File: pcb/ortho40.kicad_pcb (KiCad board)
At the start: 2 copper layers, 284 x 84 mm, 129 parts, among them J1 SWD, J2 USB_C_Receptacle_USB2.0, SW1 SW_Push, U1 RP2040, U2 XC6206PxxxMR, U3 W25Q128JVS, U4 USBLC6-2SC6, U5 ST7735S_1.8inch, Y1 12MHz

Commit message: More changes...
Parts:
- removed C1: 100nF, Capacitor_SMD:C_0402_1005Metric
- added REF**: MountingHole_2.2mm_M2, MountingHole:MountingHole_2.2mm_M2, F.Cu at (60.1, 80.1)
- added REF**: MountingHole_2.2mm_M2, MountingHole:MountingHole_2.2mm_M2, F.Cu at (60.0, 40.1)
- added REF**: MountingHole_2.2mm_M2, MountingHole:MountingHole_2.2mm_M2, F.Cu at (300.1, 40.0)
- added REF**: MountingHole_2.2mm_M2, MountingHole:MountingHole_2.2mm_M2, F.Cu at (300.2, 80.3)
- moved R2 1.47 mm to (182.8, 32.8)
- moved R3 1.03 mm to (179.1, 32.8)
- renumbered MX8 to MX10, MX10 to MX11, MX15 to MX14, MX14 to MX15, MX19 to MX18, MX21 to MX19, MX3 to MX2, MX23 to MX20, MX18 to MX21, MX20 to MX22, MX22 to MX23, MX27 to MX26, MX26 to MX27, MX2 to MX3, MX31 to MX30, MX33 to MX31, MX35 to MX32, MX30 to MX33, MX32 to MX34, MX34 to MX35, MX39 to MX38, MX38 to MX39, MX43 to MX42, MX45 to MX43, MX47 to MX44, MX42 to MX45, MX44 to MX46, MX46 to MX47, MX7 to MX6, MX9 to MX7, MX11 to MX8, MX6 to MX9
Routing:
- net r0: track 305.8 -> 304.4 mm
- net Net-(R2-Pad1): track 15.2 -> 15.9 mm

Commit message: Missing connection...
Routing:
- net QSPI_SD1: track 28.0 -> 29.0 mm
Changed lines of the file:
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@@
   (segment (start 186.90639 40.401008) (end 186.907398 40.4) (width 0.2) (layer "B.Cu") (net 97))
   (segment (start 192 35) (end 188.635 31.635) (width 0.2) (layer "B.Cu") (net 97))
-  (segment (start 187 41) (end 182.2 45.8) (width 0.2) (layer "B.Cu") (net 98))
-  (segment (start 191.4625 30.3) (end 191.4625 29.394684) (width 0.2) (layer "B.Cu") (net 98))
-  (segment (start 192 34.434314) (end 191.4625 33.896814) (width 0.2) (layer "B.Cu") (net 98))
-  (segment (start 190 41) (end 187 41) (width 0.2) (layer "B.Cu") (net 98))
-  (segment (start 188.185153 28.814847) (end 187.49375 29.50625) (width 0.2) (layer "B.Cu") (net 98))
-  (segment (start 182.2 45.8) (end 182.2 46.5625) (width 0.2) (layer "B.Cu") (net 98))
-  (segment (start 192 34.434314) (end 192.4 34.834315) (width 0.2) (layer "B.Cu") (net 98))
-  (segment (start 192.4 38.6) (end 190 41) (width 0.2) (layer "B.Cu") (net 98))
+  (segment (start 192.4 38.6) (end 192.4 34.834315) (width 0.2) (layer "B.Cu") (net 98))
+  (segment (start 187.365 29.635) (end 187.365 30.4) (width 0.2) (layer "B.Cu") (net 98))
+  (segment (start 190 41) (end 192.4 38.6) (width 0.2) (layer "B.Cu") (net 98))
+  (segment (start 182.2 45.8) (end 187 41) (width 0.2) (layer "B.Cu") (net 98))
   (segment (start 190.882663 28.814847) (end 188.185153 28.814847) (width 0.2) (layer "B.Cu") (net 98))
-  (segment (start 191.4625 33.896814) (end 191.4625 30.3) (width 0.2) (layer "B.Cu") (net 98))
-  (segment (start 192.4 34.834315) (end 192.4 38.6) (width 0.2) (layer "B.Cu") (net 98))
+  (segment (start 187 41) (end 190 41) (width 0.2) (layer "B.Cu") (net 98))
+  (segment (start 191.4625 33.896814) (end 191.4625 29.394684) (width 0.2) (layer "B.Cu") (net 98))
+  (segment (start 182.2 46.5625) (end 182.2 45.8) (width 0.2) (layer "B.Cu") (net 98))
   (segment (start 191.4625 29.394684) (end 190.882663 28.814847) (width 0.2) (layer "B.Cu") (net 98))
+  (segment (start 188.185153 28.814847) (end 187.365 29.635) (width 0.2) (layer "B.Cu") (net 98))
+  (segment (start 192.4 34.834315) (end 191.4625 33.896814) (width 0.2) (layer "B.Cu") (net 98))
   (segment (start 185.25 73.25) (end 183 71) (width 0.2) (layer "B.Cu") (net 99))
   (segment (start 173 56) (end 175 54) (width 0.2) (layer "B.Cu") (net 99))

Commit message: Use the correct footprint for the display
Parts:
- added C1: 100nF, Capacitor_SMD:C_0402_1005Metric, B.Cu at (183.3, 38.0)
- added C7: 10uF, Capacitor_SMD:C_0402_1005Metric, B.Cu at (173.0, 38.9)
- added G***: LOGO, LOGO, F.Cu at (179.4, 84.1)
- SW1: footprint Connector_PinHeader_2.54mm:PinHeader_1x02_P2.54mm_Vertical -> Button_Switch_SMD:SW_SPST_CK_KXT3; moved to B.Cu
- U5: footprint Footprints:ST7735_1.8inch -> Footprints:DFR0928; moved to F.Cu
- moved U5 27.9 mm to (197.0, 27.6), turned to 180 degrees
- moved C13 20.2 mm to (178.6, 58.4), turned to -135 degrees
- moved C4 14.5 mm to (176.4, 43.1), turned to 90 degrees
- moved C6 14.5 mm to (177.5, 57.4), turned to -135 degrees
- moved C10 4.19 mm to (179.1, 42.0)
- moved C8 4.04 mm to (175.0, 42.4)
- moved SW1 1.76 mm to (188.7, 23.6), turned to 180 degrees
- moved R2 0.67 mm to (182.7, 33.5)
- moved R3 0.66 mm to (179.0, 33.5)
- moved Y1 0.23 mm to (181.8, 61.9)
- renumbered C9 to C10, C10 to C11, C11 to C12, C12 to C13, C13 to C14, C14 to C15, C15 to C16, C16 to C17, C7 to C8, C8 to C9, REF** to MH1, REF** to MH2, REF** to MH3, REF** to MH4
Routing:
- net r2: track 312.0 -> 324.2 mm
- net LCD_RESET: track 44.6 -> 53.7 mm, vias 0 -> 1
- net LCD_DC: track 39.6 -> 36.2 mm
- net LCD_BACKLT: track 38.1 -> 35.3 mm
- net GND: track 92.2 -> 90.6 mm, vias 17 -> 22
- net +3V3: track 131.3 -> 132.6 mm
- net Net-(R3-Pad1): track 15.1 -> 14.0 mm
- net LCD_CS: track 40.2 -> 39.2 mm
- net /~{BOOTSEL}: track 4.98 -> 4.17 mm
- net LCD_RX: track 41.1 -> 40.4 mm
- net Net-(R2-Pad1): track 15.9 -> 15.3 mm
- net DN: track 2.61 -> 3.29 mm
- net DP: track 2.55 -> 3.19 mm
- net VBUS: track 12.4 -> 11.7 mm
- net CLK_IN: track 15.6 -> 16.2 mm
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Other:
- board text added: "LOBSTER 40"

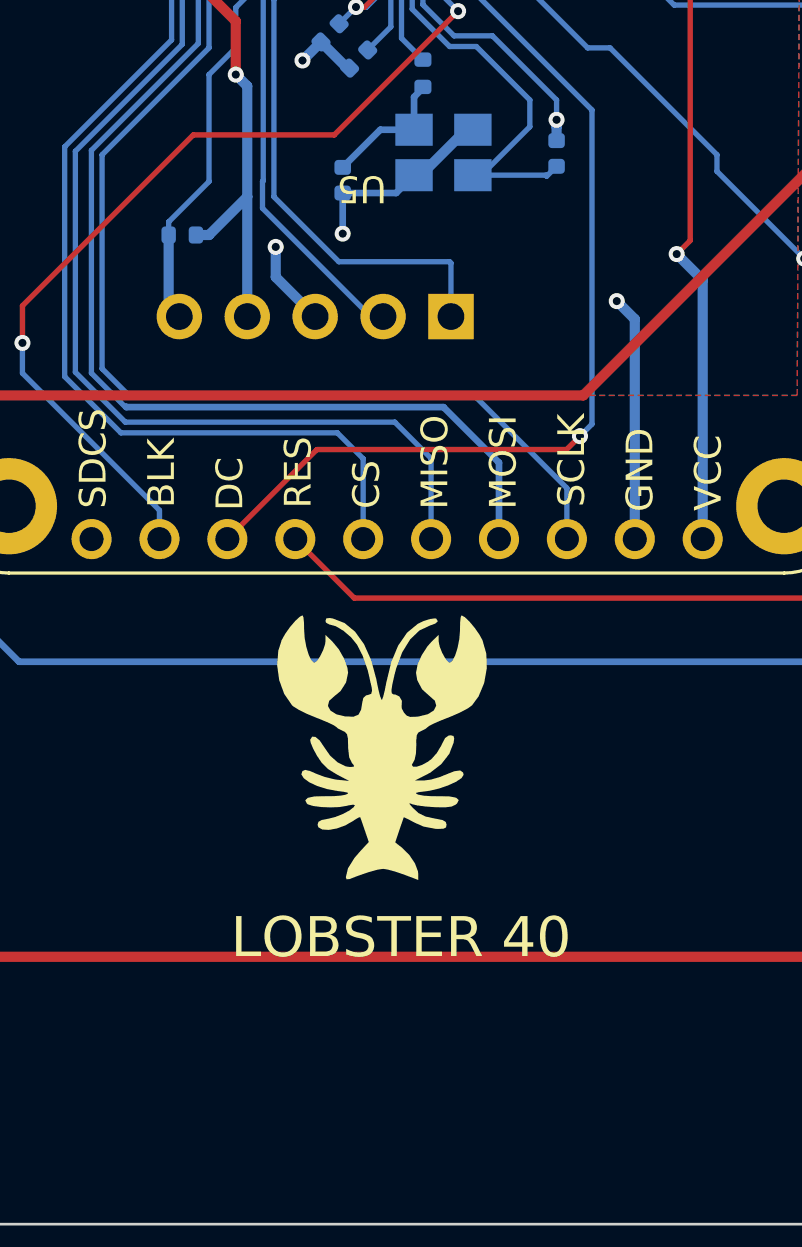
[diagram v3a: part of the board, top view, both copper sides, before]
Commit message: Clean up silkscreen
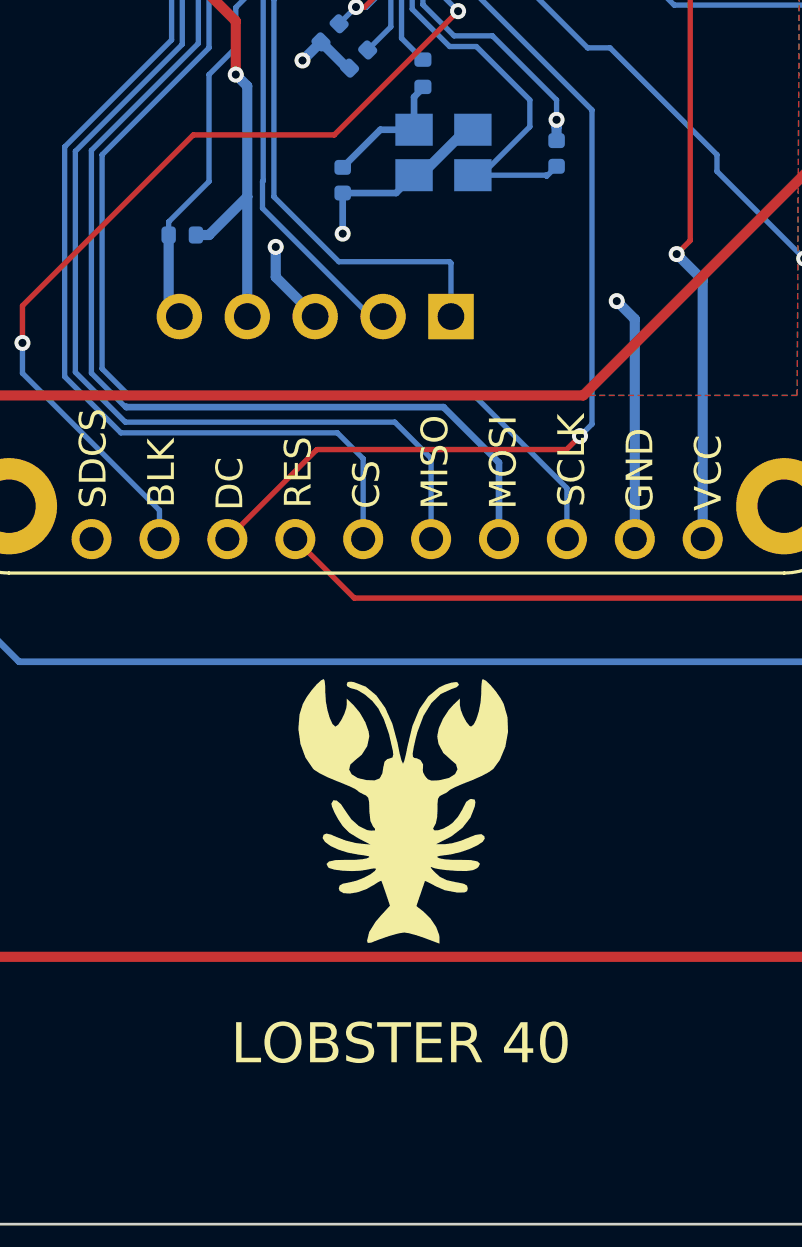
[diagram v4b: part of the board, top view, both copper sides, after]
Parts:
- moved G*** 2.51 mm to (180.2, 86.5)
- renumbered SW1 to BOOTSEL
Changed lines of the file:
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@@
   )
   (footprint "LOGO" (layer "F.Cu")
-    (at 179.3875 84.1375)
+    (at 180.18125 86.51875)
     (attr board_only exclude_from_pos_files exclude_from_bom)
     (fp_text reference "G***" (at 8.73125 0.79375) (layer "F.SilkS") hide
@@
     (property "Sheetname" "")
     (attr through_hole exclude_from_pos_files exclude_from_bom)
-    (fp_text reference "U5" (at 18.31 -35.63 180 unlocked) (layer "F.SilkS")
+    (fp_text reference "U5" (at 18.31 -35.63 180 unlocked) (layer "F.SilkS") hide
       (effects (font (size 1 1) (thickness 0.15)))
     )
@@
     (property "Sheetname" "")
     (attr smd)
-    (fp_text reference "SW1" (at 0 2) (layer "B.SilkS")
+    (fp_text reference "BOOTSEL" (at 0 2) (layer "B.SilkS")
       (effects (font (size 1 1) (thickness 0.15)) (justify mirror))
     )
@@
     (property "Sheetname" "")
     (attr smd)
-    (fp_text reference "C7" (at 0 1.16) (layer "B.SilkS")
+    (fp_text reference "C7" (at -2.295556 -0.161592) (layer "B.SilkS")
       (effects (font (size 1 1) (thickness 0.15)) (justify mirror))
     )
@@
     (property "Sheetname" "")
     (attr smd)
-    (fp_text reference "U3" (at 2.65 3.68125 90) (layer "B.SilkS")
+    (fp_text reference "U3" (at 1.71875 3.68125 90) (layer "B.SilkS") hide
       (effects (font (size 1 1) (thickness 0.15)) (justify mirror))
     )
@@
   (gr_arc (start 39 102) (mid 38.292893 101.707107) (end 38 101) (layer "Edge.Cuts") (width 0.1))
   (gr_line (start 175 18) (end 185 18) (layer "Edge.Cuts") (width 0.1))
-  (gr_text "LOBSTER 40" (at 180.18125 91.28125) (layer "F.SilkS")
+  (gr_text "LOBSTER 40" (at 180.18125 95.25) (layer "F.SilkS")
     (effects (font (size 1.5 1.5) (thickness 0.3)))
   )

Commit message: Finishing touches for rev 2
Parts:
- SW1: renamed from BOOTSEL; value SW_Push -> BOOTSEL; footprint Button_Switch_SMD:SW_SPST_CK_KXT3 -> Button_Switch_SMD:SW_Push_SPST_NO_Alps_SKRK
- moved SW1 0.77 mm to (189.4, 24.0)
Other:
- board text added: "JLCJLCJLCJLC"
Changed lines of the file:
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@@
     (property "Sheetfile" "ortho40.kicad_sch")
     (property "Sheetname" "")
-    (attr through_hole exclude_from_pos_files exclude_from_bom)
+    (attr through_hole exclude_from_pos_files)
     (fp_text reference "U5" (at 18.31 -35.63 180 unlocked) (layer "F.SilkS") hide
       (effects (font (size 1 1) (thickness 0.15)))
@@
     )
   )
-  (footprint "Button_Switch_SMD:SW_SPST_CK_KXT3" (layer "B.Cu")
-    (at 188.66281 23.644001 180)
-    (descr "https://www.ckswitches.com/media/1465/kxt3.pdf")
-    (tags "Switch SPST KXT3")
+  (footprint "Button_Switch_SMD:SW_Push_SPST_NO_Alps_SKRK" (layer "B.Cu")
+    (at 189.355943 23.974356 180)
+    (descr "http://www.alps.com/prod/info/E/HTML/Tact/SurfaceMount/SKRK/SKRKAHE020.html")
+    (tags "SMD SMT button")
     (property "Sheetfile" "ortho40.kicad_sch")
     (property "Sheetname" "")
     (attr smd)
-    (fp_text reference "BOOTSEL" (at 0 2) (layer "B.SilkS")
+    (fp_text reference "SW1" (at 0 2.543106) (layer "B.SilkS")
       (effects (font (size 1 1) (thickness 0.15)) (justify mirror))
     )
-    (fp_text value "SW_Push" (at 0 -2) (layer "B.Fab")
+    (fp_text value "BOOTSEL" (at 0 -2.5) (layer "B.Fab")
       (effects (font (size 1 1) (thickness 0.15)) (justify mirror))
     )
     (fp_text user "${REFERENCE}" (at 0 0) (layer "B.Fab")
-      (effects (font (size 0.5 0.5) (thickness 0.075)) (justify mirror))
+      (effects (font (size 1 1) (thickness 0.15)) (justify mirror))
     )
-    (fp_line (start -1.62 -1.02) (end -1.62 -1.12) (layer "B.SilkS") (width 0.12))
-    (fp_line (start -1.62 -1.12) (end 1.62 -1.12) (layer "B.SilkS") (width 0.12))
-    (fp_line (start -1.62 1.12) (end 1.62 1.12) (layer "B.SilkS") (width 0.12))
-    (fp_line (start 1.62 -1.02) (end 1.62 -1.12) (layer "B.SilkS") (width 0.12))
-    (fp_line (start 1.62 1.12) (end 1.62 1.02) (layer "B.SilkS") (width 0.12))
-    (fp_line (start -1.62 1.12) (end -1.62 1.02) (layer "B.SilkS") (width 0.12))
-    (fp_line (start -2.15 1.25) (end -2.15 -1.25) (layer "B.CrtYd") (width 0.05))
-    (fp_line (start -2.15 -1.25) (end 2.15 -1.25) (layer "B.CrtYd") (width 0.05))
-    (fp_line (start 2.15 1.25) (end 2.15 -1.25) (layer "B.CrtYd") (width 0.05))
-    (fp_line (start -2.15 1.25) (end 2.15 1.25) (layer "B.CrtYd") (width 0.05))
-    (fp_line (start 1.5 -1) (end -1.5 -1) (layer "B.Fab") (width 0.1))
-    (fp_line (start -1.5 1) (end 1.5 1) (layer "B.Fab") (width 0.1))
-    (fp_line (start 1.75 0.4) (end 1.5 0.15) (layer "B.Fab") (width 0.1))
-    (fp_line (start 1.75 0.65) (end 1.75 0.4) (layer "B.Fab") (width 0.1))
-    (fp_line (start 1.75 -0.65) (end 1.5 -0.65) (layer "B.Fab") (width 0.1))
-    (fp_line (start -1.5 -0.15) (end -1.75 -0.4) (layer "B.Fab") (width 0.1))
-    (fp_line (start -1.5 -1) (end -1.5 1) (layer "B.Fab") (width 0.1))
-    (fp_line (start 1.5 1) (end 1.5 -1) (layer "B.Fab") (width 0.1))
-    (fp_line (start 1.5 -0.15) (end 1.75 -0.4) (layer "B.Fab") (width 0.1))
-    (fp_line (start -1.75 -0.65) (end -1.5 -0.65) (layer "B.Fab") (width 0.1))
-    (fp_line (start -1.75 -0.4) (end -1.75 -0.65) (layer "B.Fab") (width 0.1))
-    (fp_line (start -1.5 0.65) (end -1.75 0.65) (layer "B.Fab") (width 0.1))
-    (fp_line (start 1.75 -0.4) (end 1.75 -0.65) (layer "B.Fab") (width 0.1))
-    (fp_line (start -1.75 0.4) (end -1.5 0.15) (layer "B.Fab") (width 0.1))
-    (fp_line (start -1.75 0.65) (end -1.75 0.4) (layer "B.Fab") (width 0.1))
-    (fp_line (start 1.5 0.65) (end 1.75 0.65) (layer "B.Fab") (width 0.1))
-    (pad "1" smd rect (at -1.625 0 180) (size 0.55 1.5) (layers "B.Cu" "B.Paste" "B.Mask")
+    (fp_line (start -2.07 -1.57) (end -2.07 -1.27) (layer "B.SilkS") (width 0.12))
+    (fp_line (start -2.07 1.57) (end 2.07 1.57) (layer "B.SilkS") (width 0.12))
+    (fp_line (start 2.07 -1.57) (end -2.07 -1.57) (layer "B.SilkS") (width 0.12))
+    (fp_line (start 2.07 -1.27) (end 2.07 -1.57) (layer "B.SilkS") (width 0.12))
+    (fp_line (start -2.07 1.27) (end -2.07 1.57) (layer "B.SilkS") (width 0.12))
+    (fp_line (start 2.07 1.57) (end 2.07 1.27) (layer "B.SilkS") (width 0.12))
+    (fp_line (start -2.75 1.7) (end 2.75 1.7) (layer "B.CrtYd") (width 0.05))
+    (fp_line (start 2.75 -1.7) (end -2.75 -1.7) (layer "B.CrtYd") (width 0.05))
+    (fp_line (start 2.75 1.7) (end 2.75 -1.7) (layer "B.CrtYd") (width 0.05))
+    (fp_line (start -2.75 -1.7) (end -2.75 1.7) (layer "B.CrtYd") (width 0.05))
+    (fp_line (start -1.95 1.45) (end 1.95 1.45) (layer "B.Fab") (width 0.1))
+    (fp_line (start 1.95 1.45) (end 1.95 -1.45) (layer "B.Fab") (width 0.1))
+    (fp_line (start 1.95 -1.45) (end -1.95 -1.45) (layer "B.Fab") (width 0.1))
+    (fp_line (start -1.95 -1.45) (end -1.95 1.45) (layer "B.Fab") (width 0.1))
+    (fp_circle (center 0 0) (end 1 0) (layer "B.Fab") (width 0.1) (fill none))
+    (pad "1" smd roundrect (at -2.1 0 180) (size 0.8 2) (layers "B.Cu" "B.Paste" "B.Mask") (roundrect_rratio 0.25)
       (net 2 "GND") (pinfunction "1") (pintype "passive"))
-    (pad "2" smd rect (at 1.625 0 180) (size 0.55 1.5) (layers "B.Cu" "B.Paste" "B.Mask")
+    (pad "2" smd roundrect (at 2.1 0 180) (size 0.8 2) (layers "B.Cu" "B.Paste" "B.Mask") (roundrect_rratio 0.25)
       (net 84 "/~{BOOTSEL}") (pinfunction "2") (pintype "passive"))
-    (model "${KICAD6_3DMODEL_DIR}/Button_Switch_SMD.3dshapes/SW_SPST_CK_KXT3.wrl"
+    (model "${KICAD6_3DMODEL_DIR}/Button_Switch_SMD.3dshapes/SW_Push_SPST_NO_Alps_SKRK.wrl"
       (offset (xyz 0 0 0))
       (scale (xyz 1 1 1))
@@
     (property "Sheetfile" "ortho40.kicad_sch")
     (property "Sheetname" "")
-    (attr through_hole exclude_from_pos_files)
-    (fp_text reference "J1" (at 0 2.77 90) (layer "B.SilkS")
+    (attr through_hole exclude_from_pos_files exclude_from_bom)
+    (fp_text reference "J1" (at 0 2.77 90) (layer "B.SilkS") hide
       (effects (font (size 1 1) (thickness 0.15)) (justify mirror))
     )
@@
   (gr_arc (start 39 102) (mid 38.292893 101.707107) (end 38 101) (layer "Edge.Cuts") (width 0.1))
   (gr_line (start 175 18) (end 185 18) (layer "Edge.Cuts") (width 0.1))
+  (gr_text "JLCJLCJLCJLC" (at 180.18125 100.0125) (layer "B.SilkS")
+    (effects (font (size 1.5 1.5) (thickness 0.3)))
+  )
   (gr_text "LOBSTER 40" (at 180.18125 95.25) (layer "F.SilkS")
     (effects (font (size 1.5 1.5) (thickness 0.3)))
@@
   (segment (start 180.05 31.951204) (end 179.006966 32.994238) (width 0.381) (layer "B.Cu") (net 83))
   (segment (start 180.05 30.1375) (end 180.05 31.951204) (width 0.381) (layer "B.Cu") (net 83))
+  (segment (start 187.03781 26.39122) (end 187.03781 24.192489) (width 0.25) (layer "B.Cu") (net 84))
   (segment (start 186.034799 27.394231) (end 187.03781 26.39122) (width 0.25) (layer "B.Cu") (net 84))
-  (segment (start 187.03781 26.39122) (end 187.03781 23.644001) (width 0.25) (layer "B.Cu") (net 84))
+  (segment (start 187.03781 24.192489) (end 187.255943 23.974356) (width 0.25) (layer "B.Cu") (net 84))
   (segment (start 193.036904 38.528782) (end 190.165686 41.4) (width 0.2) (layer "B.Cu") (net 85))
   (segment (start 192.0875 33.956128) (end 192.0875 29.36875) (width 0.2) (layer "B.Cu") (net 85))
